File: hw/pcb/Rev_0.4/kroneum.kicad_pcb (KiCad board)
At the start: 2 copper layers, 43.7 x 40 mm, 23 parts, among them J1 USB_B_Micro, SW1 Boot_Mode_Btn, SW2 Ctrl_One_Btn, SW3 Reset_Btn, SW4 Ctrl_Ten_Btn, U1 STM32F042F4Px, U2 MCP1700-3302E_SOT89

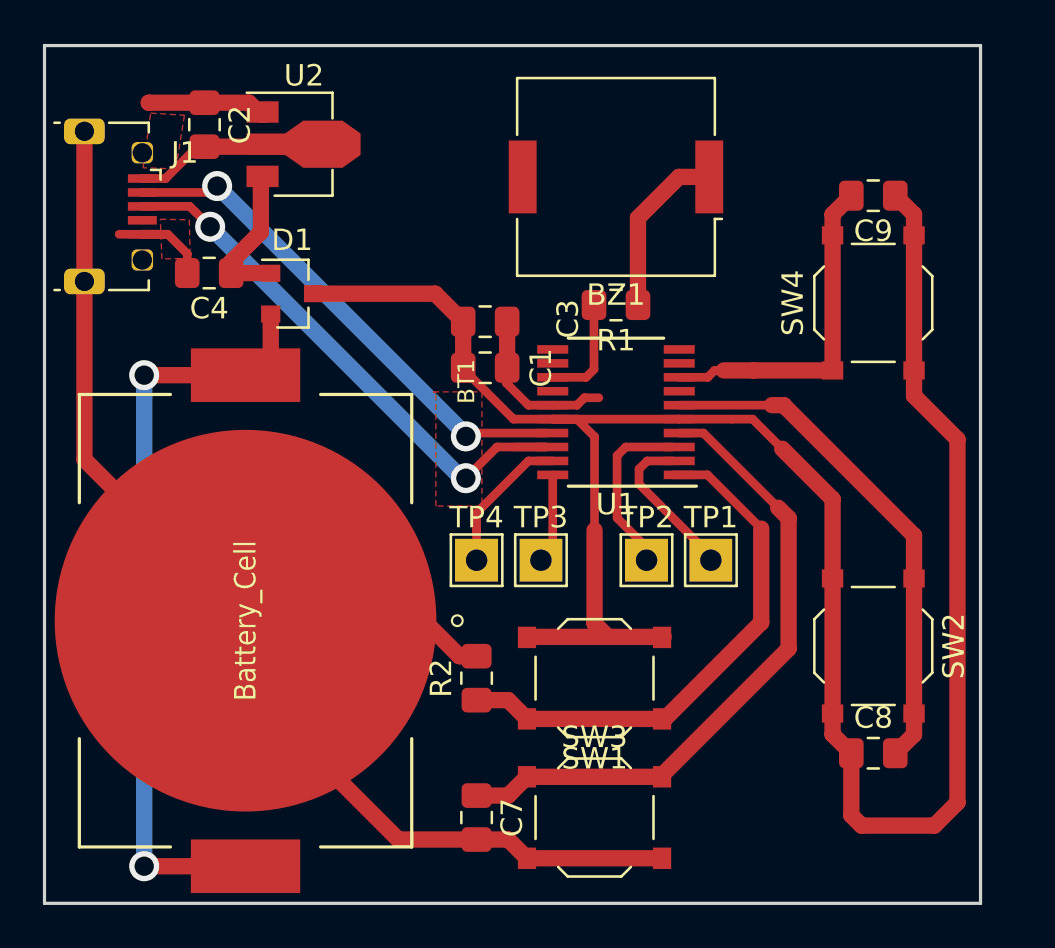
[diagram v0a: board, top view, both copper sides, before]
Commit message: hw: fix DRC errors.
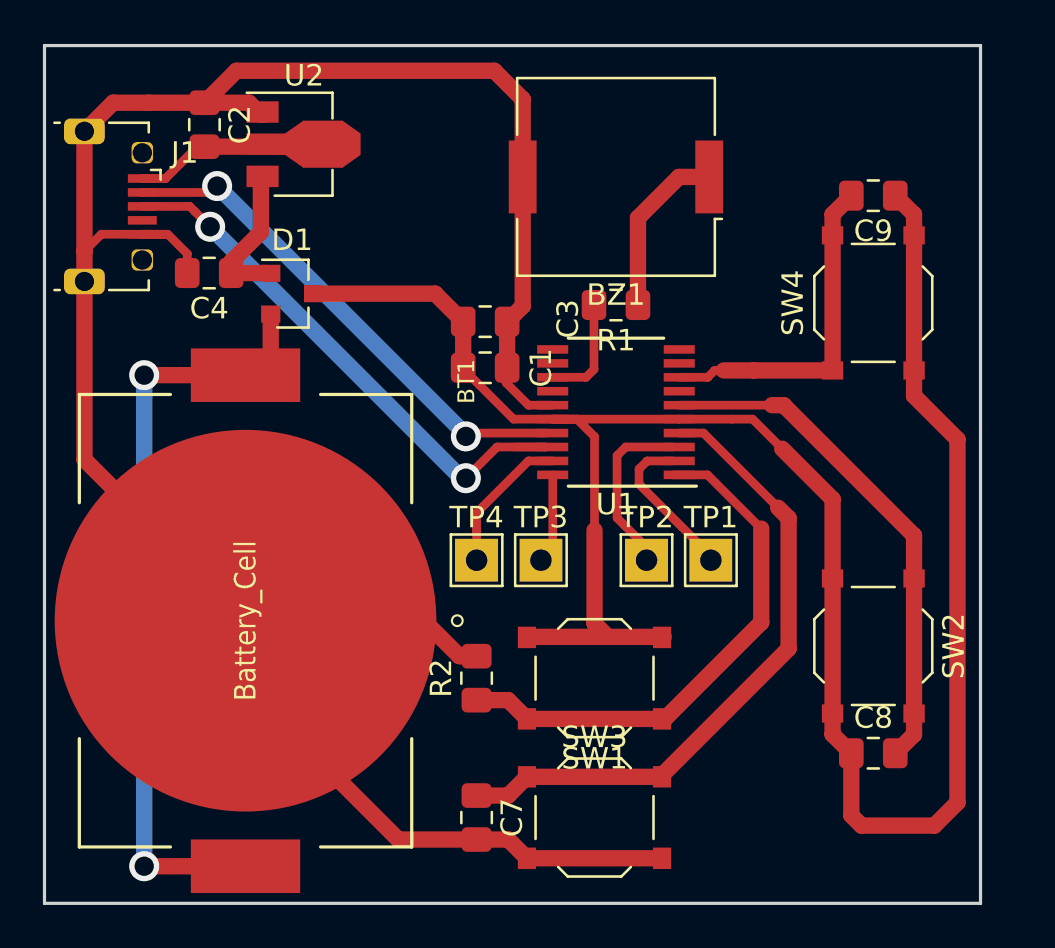
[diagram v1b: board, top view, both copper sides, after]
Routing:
- net GND: track 83.8 -> 112.6 mm
- removed copper zone on F.Cu, net GND
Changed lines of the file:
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@@
     (thickness 1.6)
     (drawings 4)
-    (tracks 158)
+    (tracks 163)
     (zones 0)
     (modules 23)
@@
   )
   (setup
-    (last_trace_width 0.25)
+    (last_trace_width 0.762)
     (user_trace_width 0.4064)
     (user_trace_width 0.4572)
@@
   (gr_line (start 121.35 133) (end 121.35 93) (layer Edge.Cuts) (width 0.15))
   (segment (start 125.9125 101.8) (end 126.3875 101.8) (width 0.4064) (layer F.Cu) (net 1))
-  (segment (start 126.215 95.665) (end 128.81 95.665) (width 0.762) (layer F.Cu) (net 1))
   (segment (start 126.21 95.67) (end 126.215 95.665) (width 0.762) (layer F.Cu) (net 1))
   (segment (start 143.9186 109.77) (end 142.875 108.7264) (width 0.4064) (layer F.Cu) (net 1))
@@
   (segment (start 130.885 95.665) (end 131.44 96.22) (width 0.762) (layer F.Cu) (net 1))
   (segment (start 128.81 95.665) (end 130.885 95.665) (width 0.762) (layer F.Cu) (net 1))
-  (segment (start 143.65 98.075) (end 143.65 99.125) (width 0.762) (layer F.Cu) (net 1))
   (segment (start 131.44 96.22) (end 131.69 96.22) (width 0.762) (layer F.Cu) (net 1))
   (segment (start 142.925 105.875) (end 142.925 108.025) (width 0.762) (layer F.Cu) (net 1))
-  (segment (start 123.2125 97) (end 123.2125 104) (width 0.762) (layer F.Cu) (net 1))
   (segment (start 123.2125 112.3075) (end 130.725 119.82) (width 0.762) (layer F.Cu) (net 1))
   (segment (start 123.2125 104) (end 123.2125 112.3075) (width 0.762) (layer F.Cu) (net 1))
@@
   (segment (start 130.725 122.9) (end 130.725 119.82) (width 0.762) (layer F.Cu) (net 1))
   (segment (start 137.85 130.025) (end 130.725 122.9) (width 0.762) (layer F.Cu) (net 1))
-  (segment (start 125.9125 101.8) (end 124.8311 101.8) (width 0.4064) (layer F.Cu) (net 1))
   (segment (start 142.975 130.025) (end 143.85 130.9) (width 0.762) (layer F.Cu) (net 1))
   (segment (start 141.5 130.025) (end 142.975 130.025) (width 0.762) (layer F.Cu) (net 1))
@@
   (segment (start 125.9125 101.8) (end 127.1 101.8) (width 0.4064) (layer F.Cu) (net 1))
   (segment (start 127.1 101.8) (end 128.007 102.707) (width 0.4064) (layer F.Cu) (net 1))
-  (segment (start 146.1814 109.77) (end 146.5264 109.425) (width 0.4064) (layer F.Cu) (net 1))
-  (segment (start 145.05 109.77) (end 146.1814 109.77) (width 0.4064) (layer F.Cu) (net 1))
-  (segment (start 146.5264 109.425) (end 147.2 109.425) (width 0.4064) (layer F.Cu) (net 1))
+  (segment (start 124 101.8) (end 123.2125 102.5875) (width 0.4064) (layer F.Cu) (net 1))
+  (segment (start 123.2125 97) (end 123.2125 102.5875) (width 0.762) (layer F.Cu) (net 1))
+  (segment (start 125.9125 101.8) (end 124 101.8) (width 0.4064) (layer F.Cu) (net 1))
+  (segment (start 123.2125 102.5875) (end 123.2125 104) (width 0.762) (layer F.Cu) (net 1))
+  (segment (start 124.5475 95.665) (end 128.81 95.665) (width 0.762) (layer F.Cu) (net 1))
+  (segment (start 123.2125 97) (end 124.5475 95.665) (width 0.762) (layer F.Cu) (net 1))
+  (segment (start 143.65 95.5) (end 143.65 99.125) (width 0.762) (layer F.Cu) (net 1))
+  (segment (start 128.81 95.665) (end 130.3 94.175) (width 0.762) (layer F.Cu) (net 1))
+  (segment (start 142.325 94.175) (end 143.65 95.5) (width 0.762) (layer F.Cu) (net 1))
+  (segment (start 130.3 94.175) (end 142.325 94.175) (width 0.762) (layer F.Cu) (net 1))
+  (segment (start 143.65 105.15) (end 142.925 105.875) (width 0.762) (layer F.Cu) (net 1))
+  (segment (start 143.65 99.125) (end 143.65 105.15) (width 0.762) (layer F.Cu) (net 1))
   (segment (start 150.938 99.125) (end 152.35 99.125) (width 0.762) (layer F.Cu) (net 2))
   (segment (start 149.025 101.038) (end 150.938 99.125) (width 0.762) (layer F.Cu) (net 2))
@@
   (segment (start 131.44 99.22) (end 131.44 101.7) (width 0.762) (layer F.Cu) (net 24))
   (segment (start 131.44 101.7) (end 130.057 103.083) (width 0.762) (layer F.Cu) (net 24))
-  (zone (net 1) (net_name GND) (layer F.Cu) (hatch none 0.508)
-    (connect_pads (clearance 0.5))
-    (min_thickness 0.3)
-    (fill yes (arc_segments 32) (thermal_gap 0.6) (thermal_bridge_width 0.6))
-    (polygon
-      (pts
-        (xy 121.375 93.025) (xy 165 93) (xy 165 133) (xy 121.35 132.975)
-      )
-    )
-    (polygon
-      (pts
-        (xy 126.75 101.1) (xy 128.1 101.125) (xy 128.15 102.925) (xy 126.825 102.95)
-      )
-    )
-    (polygon
-      (pts
-        (xy 126.3 96.15) (xy 127.875 96.25) (xy 127.475 98.75) (xy 125.95 98.7)
-      )
-    )
-    (polygon
-      (pts
-        (xy 139.475 109.15) (xy 141.75 109.15) (xy 141.75 114.475) (xy 139.6 114.475) (xy 139.6 109.2)
-      )
-    )
-  )
 )

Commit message: hw: finish Rev 0.4 PCB layout.
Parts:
- SW1: value Boot_Mode_Btn -> Boot
- SW2: value Ctrl_One_Btn -> One
- SW3: value Reset_Btn -> Reset
- SW4: value Ctrl_Ten_Btn -> Ten
- TP1, TP2, TP3, TP4: moved to B.Cu
- moved TP4 10.8 mm to (149.6, 109.9), turned to 180 degrees
- moved TP2 8.26 mm to (153.6, 109.9), turned to 180 degrees
- moved C7 7.87 mm to (148.0, 124.6), turned to 180 degrees
- moved R2 6.53 mm to (148.0, 122.5), turned to 180 degrees
- moved TP3 5.91 mm to (149.6, 113.9), turned to 180 degrees
- moved C8 5.21 mm to (159.7, 120.8)
- moved C9 5.11 mm to (159.7, 105.1), turned to 0 degrees
- moved SW4 5.11 mm to (159.7, 99.9), turned to 270 degrees
- moved SW2 5.01 mm to (159.7, 126.0)
- moved SW1 4.66 mm to (148.0, 118.0)
- moved BT1 3.58 mm to (134.3, 119.8)
- moved J1 3.58 mm to (128.0, 100.5)
- moved C1 3.58 mm to (145.5, 108.0)
- moved C2 3.58 mm to (132.4, 96.6)
- moved C3 3.58 mm to (145.5, 105.8)
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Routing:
- net VDD: track 103.7 -> 77.4 mm
- net GND: track 112.6 -> 120.2 mm
- net SCL: track 8.21 -> 3.92 mm, vias 0 -> 1
- net SDA: track 7.92 -> 3.86 mm, vias 0 -> 1
- net SWDIO: track 6.76 -> 4.19 mm, vias 0 -> 1
- net Ctrl_Ten: track 15.8 -> 18.0 mm
- net Net-(BZ1-Pad1): track 8.18 -> 7.22 mm
- net Ctrl_One: track 24.0 -> 24.8 mm
- net BOOT0: track 25.1 -> 24.3 mm
- net Buzzer: track 5.38 -> 5.95 mm
- net SWCLK: track 4.21 -> 4.31 mm, vias 0 -> 1
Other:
- board size 43.7 x 40 mm -> 40 x 40 mm

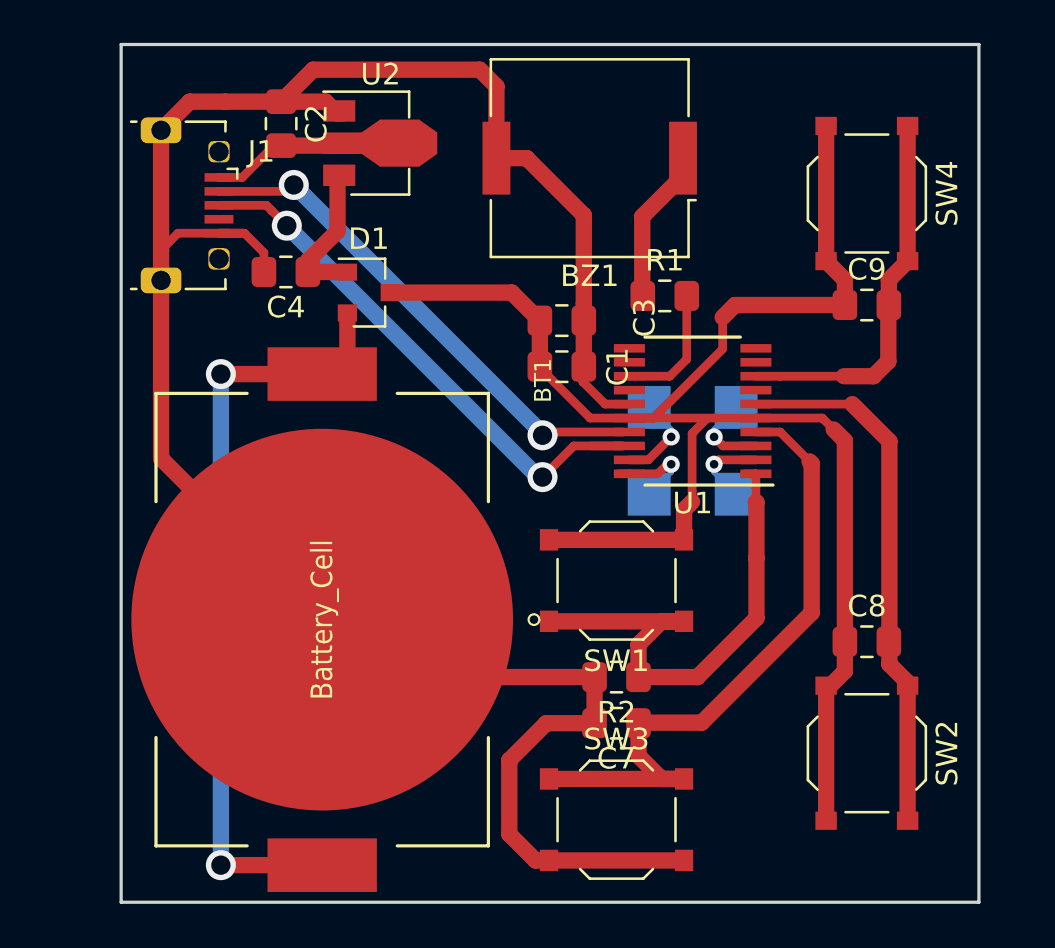
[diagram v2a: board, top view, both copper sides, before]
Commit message: hw: improve PCB to allow USB port be outside of PCB and avoid collisions with the enclosure and USB cable.
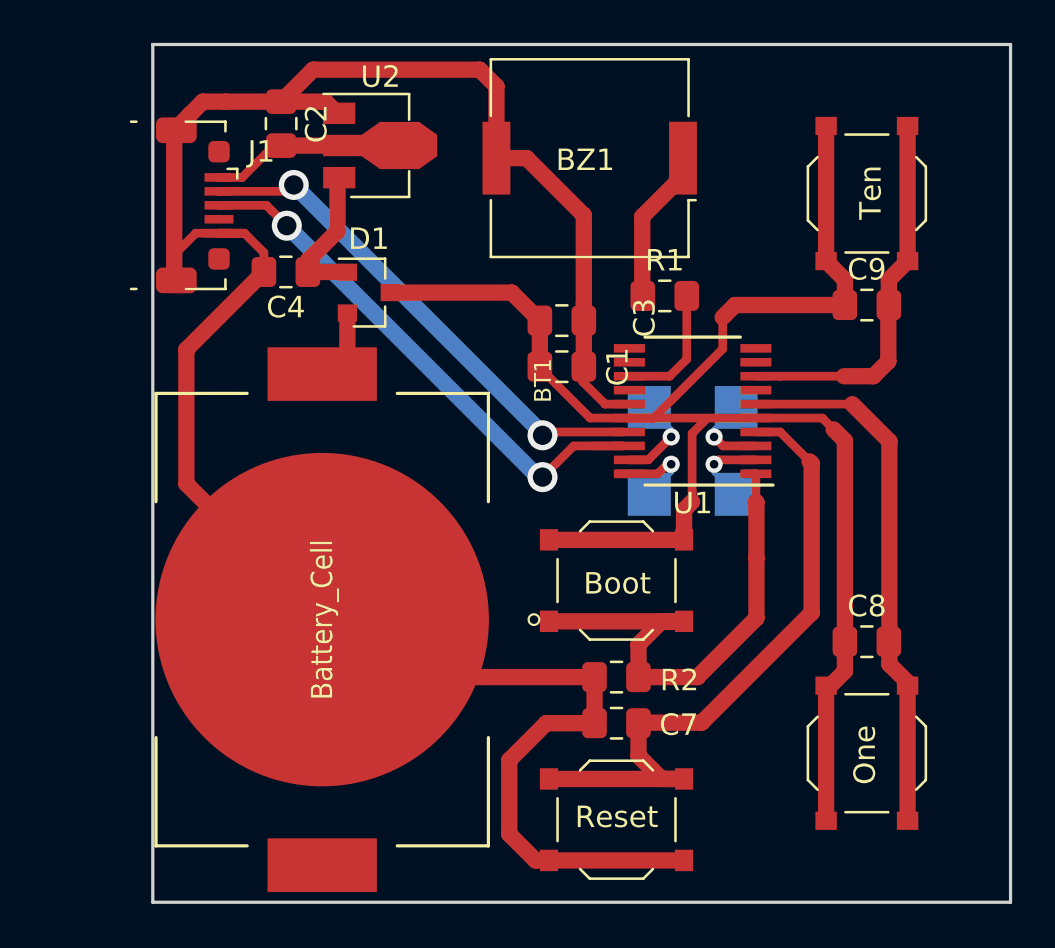
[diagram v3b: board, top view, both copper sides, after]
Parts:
- moved U2 0.11 mm to (136.6, 97.7)
- renumbered SW1 to Boot, SW2 to One, SW3 to Reset, SW4 to Ten
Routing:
- net Net-(BT1-Pad1): track 34.0 -> 1.67 mm, vias 2 -> 0
- net GND: track 120.2 -> 106.8 mm
